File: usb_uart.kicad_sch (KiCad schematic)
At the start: 10 parts, among them U401 FT232RL, U402 CH340C

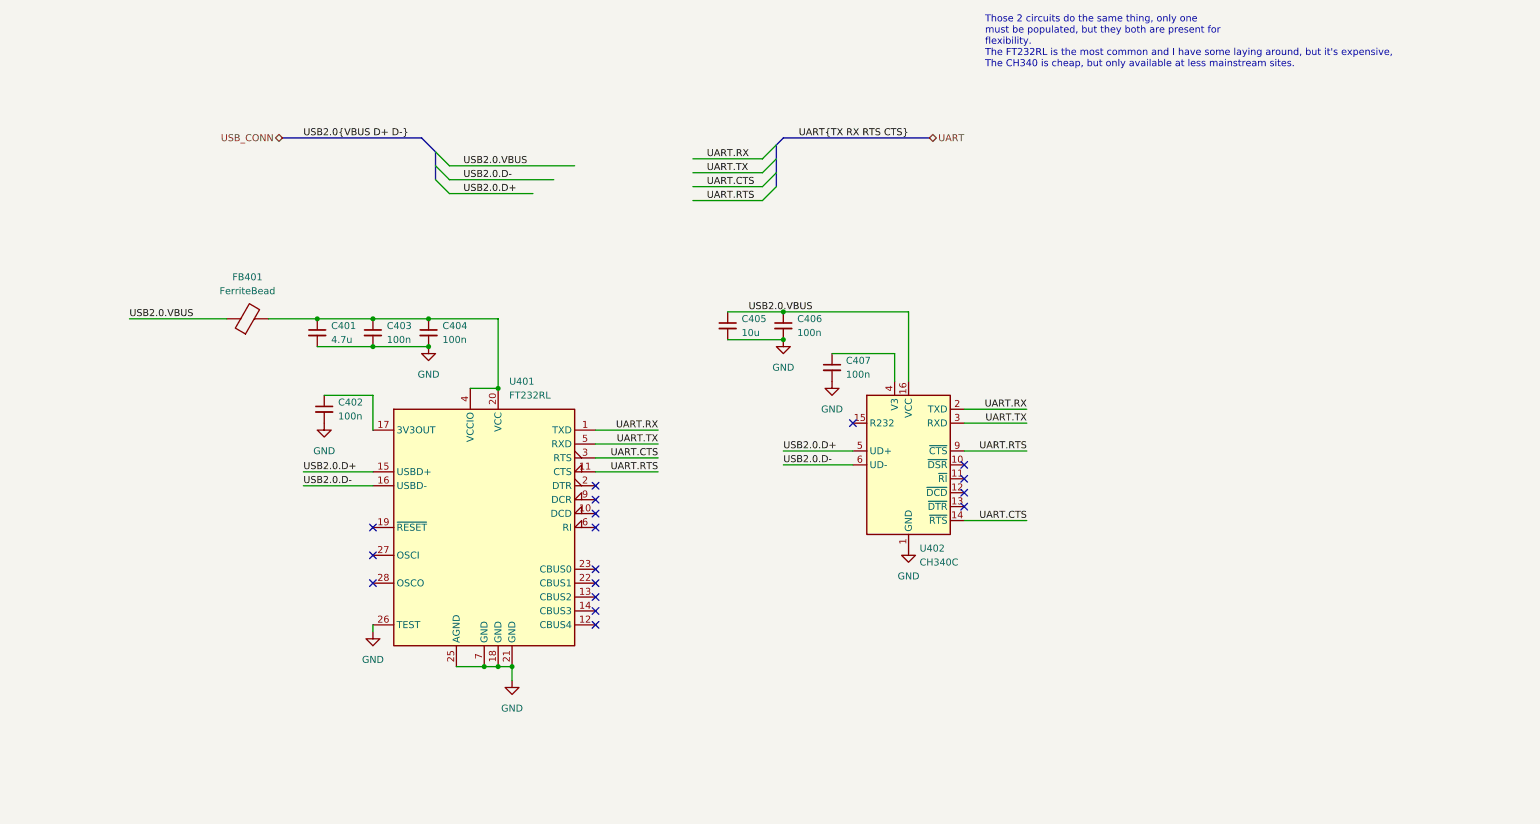
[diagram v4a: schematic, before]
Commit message: Add partnumbers
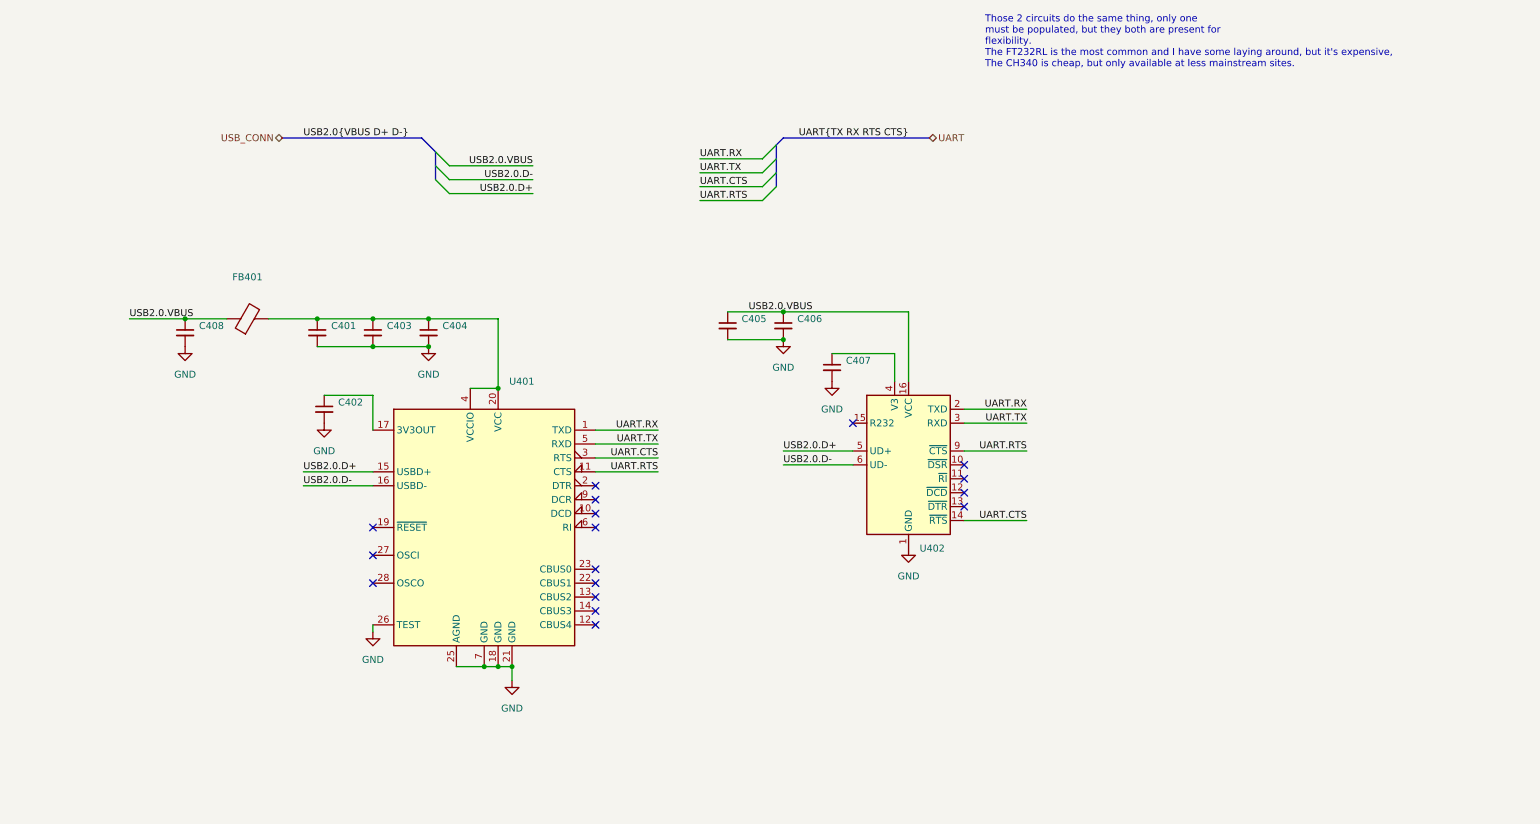
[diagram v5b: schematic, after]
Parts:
- added C408: (no value), symbol Device:C_Small
- C401: value 4.7u -> (none); footprint Capacitor_SMD:C_0805_2012Metric -> (none); Manufacturer (none) -> Generic; PartNumber (none) -> Generic
- C402, C403, C404, C406, C407: value 100n -> (none); footprint Capacitor_SMD:C_0402_1005Metric -> (none); Manufacturer (none) -> Generic; PartNumber (none) -> Generic
- C405: value 10u -> (none); footprint Capacitor_SMD:C_0805_2012Metric -> (none); Manufacturer (none) -> Generic; PartNumber (none) -> Generic
- FB401: value FerriteBead -> (none); footprint Inductor_SMD:L_0805_2012Metric -> (none); Manufacturer (none) -> Bourns; PartNumber (none) -> MH2029-400Y
- U401: value FT232RL -> (none); footprint Package_SO:SSOP-28_5.3x10.2mm_P0.65mm -> (none); Manufacturer (none) -> FTDI; PartNumber (none) -> FT232RL
- U402: value CH340C -> (none); footprint Package_SO:SOIC-16_3.9x9.9mm_P1.27mm -> (none); Manufacturer (none) -> WCH; PartNumber (none) -> CH340C
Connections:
- net GND: now also C408.2
- net USB2.0.VBUS: now also C408.1

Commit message: Fix missing footprints in schematic
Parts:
- C401, C402, C403, C404, C405, C406, C407, C408: now left out of the parts list
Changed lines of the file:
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@@
   )
   (symbol (lib_id "Device:C_Small") (at 73.66 87.63 0) (unit 1)
-    (in_bom yes) (on_board yes) (fields_autoplaced)
+    (in_bom no) (on_board yes) (fields_autoplaced)
     (property "Reference" "C402" (id 0) (at 76.2 86.3662 0)
       (effects (font (size 1.27 1.27)) (justify left))
@@
   )
   (symbol (lib_id "Device:C_Small") (at 82.55 73.66 0) (unit 1)
-    (in_bom yes) (on_board yes) (fields_autoplaced)
+    (in_bom no) (on_board yes) (fields_autoplaced)
     (property "Reference" "C403" (id 0) (at 85.09 72.3962 0)
       (effects (font (size 1.27 1.27)) (justify left))
@@
   )
   (symbol (lib_id "Device:C_Small") (at 166.37 80.01 0) (unit 1)
-    (in_bom yes) (on_board yes) (fields_autoplaced)
+    (in_bom no) (on_board yes) (fields_autoplaced)
     (property "Reference" "C407" (id 0) (at 168.91 78.7462 0)
       (effects (font (size 1.27 1.27)) (justify left))
@@
   )
   (symbol (lib_id "Device:C_Small") (at 147.32 72.39 0) (unit 1)
-    (in_bom yes) (on_board yes) (fields_autoplaced)
+    (in_bom no) (on_board yes) (fields_autoplaced)
     (property "Reference" "C405" (id 0) (at 149.86 71.1262 0)
       (effects (font (size 1.27 1.27)) (justify left))
@@
   )
   (symbol (lib_id "Device:C_Small") (at 157.48 72.39 0) (unit 1)
-    (in_bom yes) (on_board yes) (fields_autoplaced)
+    (in_bom no) (on_board yes) (fields_autoplaced)
     (property "Reference" "C406" (id 0) (at 160.02 71.1262 0)
       (effects (font (size 1.27 1.27)) (justify left))
@@
   )
   (symbol (lib_id "Device:C_Small") (at 92.71 73.66 0) (unit 1)
-    (in_bom yes) (on_board yes) (fields_autoplaced)
+    (in_bom no) (on_board yes) (fields_autoplaced)
     (property "Reference" "C404" (id 0) (at 95.25 72.3962 0)
       (effects (font (size 1.27 1.27)) (justify left))
@@
   )
   (symbol (lib_id "Device:C_Small") (at 48.26 73.66 0) (unit 1)
-    (in_bom yes) (on_board yes) (fields_autoplaced)
+    (in_bom no) (on_board yes) (fields_autoplaced)
     (property "Reference" "C408" (id 0) (at 50.8 72.3962 0)
       (effects (font (size 1.27 1.27)) (justify left))
@@
   )
   (symbol (lib_id "Device:C_Small") (at 72.39 73.66 0) (unit 1)
-    (in_bom yes) (on_board yes) (fields_autoplaced)
+    (in_bom no) (on_board yes) (fields_autoplaced)
     (property "Reference" "C401" (id 0) (at 74.93 72.3962 0)
       (effects (font (size 1.27 1.27)) (justify left))

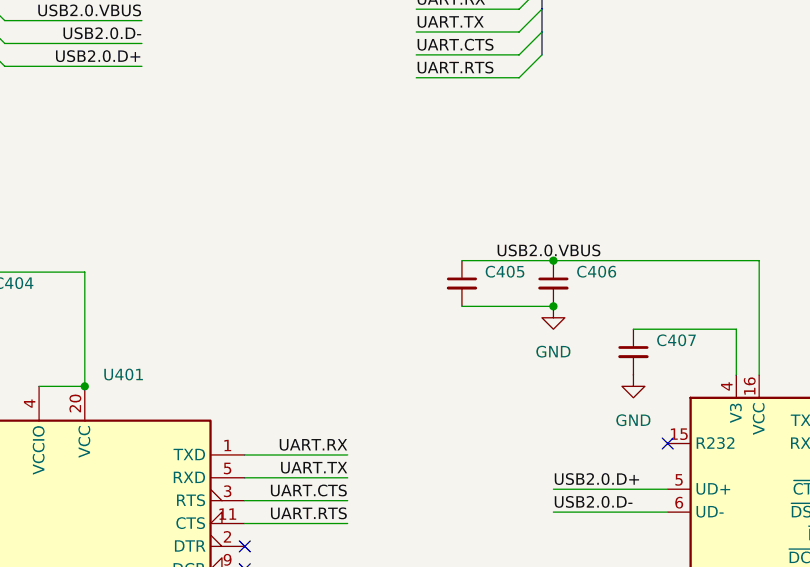
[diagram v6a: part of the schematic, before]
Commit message: Change some partnumbers in preparation for the order
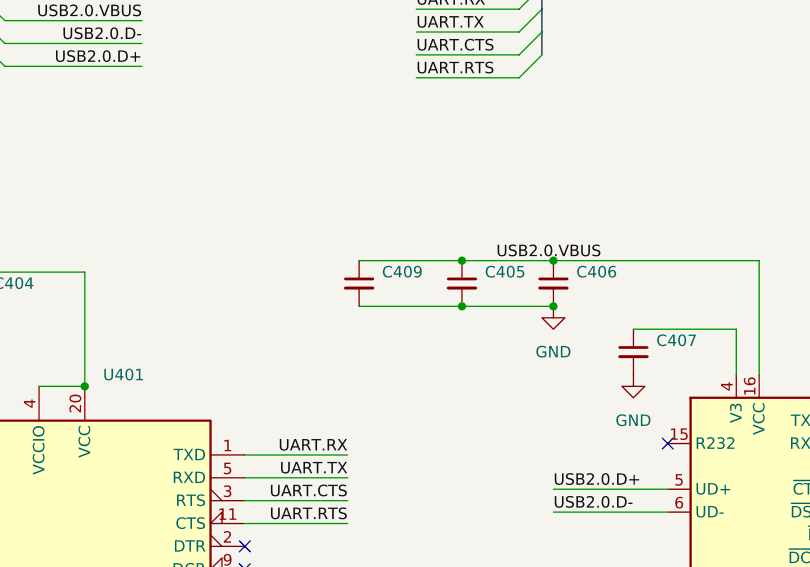
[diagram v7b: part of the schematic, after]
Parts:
- added C409: (no value), symbol Device:C_Small
- U402: now left out of the parts list
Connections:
- net GND: now also C409.2
- net USB2.0.VBUS: now also C409.1
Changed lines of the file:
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@@
   (junction (at 102.87 134.62) (diameter 0) (color 0 0 0 0)
   )
+  (junction (at 147.32 74.93) (diameter 0) (color 0 0 0 0)
+  )
   (junction (at 105.41 83.82) (diameter 0) (color 0 0 0 0)
   )
@@
   )
   (junction (at 157.48 74.93) (diameter 0) (color 0 0 0 0)
+  )
+  (junction (at 147.32 69.85) (diameter 0) (color 0 0 0 0)
   )
   (no_connect (at 190.5 97.79))
@@
     (stroke (width 0) (type default) (color 0 0 0 0))
   )
+  (wire (pts (xy 135.89 74.93) (xy 147.32 74.93))
+    (stroke (width 0) (type default) (color 0 0 0 0))
+  )
   (bus (pts (xy 157.48 38.1) (xy 156.21 39.37))
     (stroke (width 0) (type default) (color 0 0 0 0))
@@
   )
   (wire (pts (xy 123.19 91.44) (xy 134.62 91.44))
+    (stroke (width 0) (type default) (color 0 0 0 0))
+  )
+  (wire (pts (xy 135.89 69.85) (xy 147.32 69.85))
     (stroke (width 0) (type default) (color 0 0 0 0))
   )
@@
   )
   (symbol (lib_id "Interface_USB:CH340C") (at 180.34 97.79 0) (unit 1)
-    (in_bom yes) (on_board yes) (fields_autoplaced)
+    (in_bom no) (on_board yes) (fields_autoplaced)
     (property "Reference" "U402" (id 0) (at 182.3594 113.03 0)
       (effects (font (size 1.27 1.27)) (justify left))
@@
       (effects (font (size 1.27 1.27)) hide)
     )
+    (pin "1")
+    (pin "2")
+  )
+  (symbol (lib_id "Device:C_Small") (at 135.89 72.39 0) (unit 1)
+    (in_bom no) (on_board yes) (fields_autoplaced)
+    (property "Reference" "C409" (id 0) (at 138.43 71.1262 0)
+      (effects (font (size 1.27 1.27)) (justify left))
+    )
+    (property "Value" "" (id 1) (at 138.43 73.6662 0)
+      (effects (font (size 1.27 1.27)) (justify left))
+    )
+    (property "Footprint" "" (id 2) (at 135.89 72.39 0)
+      (effects (font (size 1.27 1.27)) hide)
+    )
+    (property "Datasheet" "~" (id 3) (at 135.89 72.39 0)
+      (effects (font (size 1.27 1.27)) hide)
+    )
+    (property "Manufacturer" "Generic" (id 4) (at 135.89 72.39 0)
+      (effects (font (size 1.27 1.27)) hide)
+    )
+    (property "PartNumber" "Generic" (id 5) (at 135.89 72.39 0)
+      (effects (font (size 1.27 1.27)) hide)
+    )
